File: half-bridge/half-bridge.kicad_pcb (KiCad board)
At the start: 4 copper layers, 59 x 36 mm, 96 parts, among them J1 Conn_01x11_Pin, J2 MountingHole_Pad, J3 Conn_01x11_Pin, J4 Conn_01x11_Pin, J5 Conn_01x11_Pin, J6 Conn_01x11_Pin, J7 MountingHole_Pad, J8 MountingHole_Pad, J9 MountingHole_Pad, Q1 EPC2306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

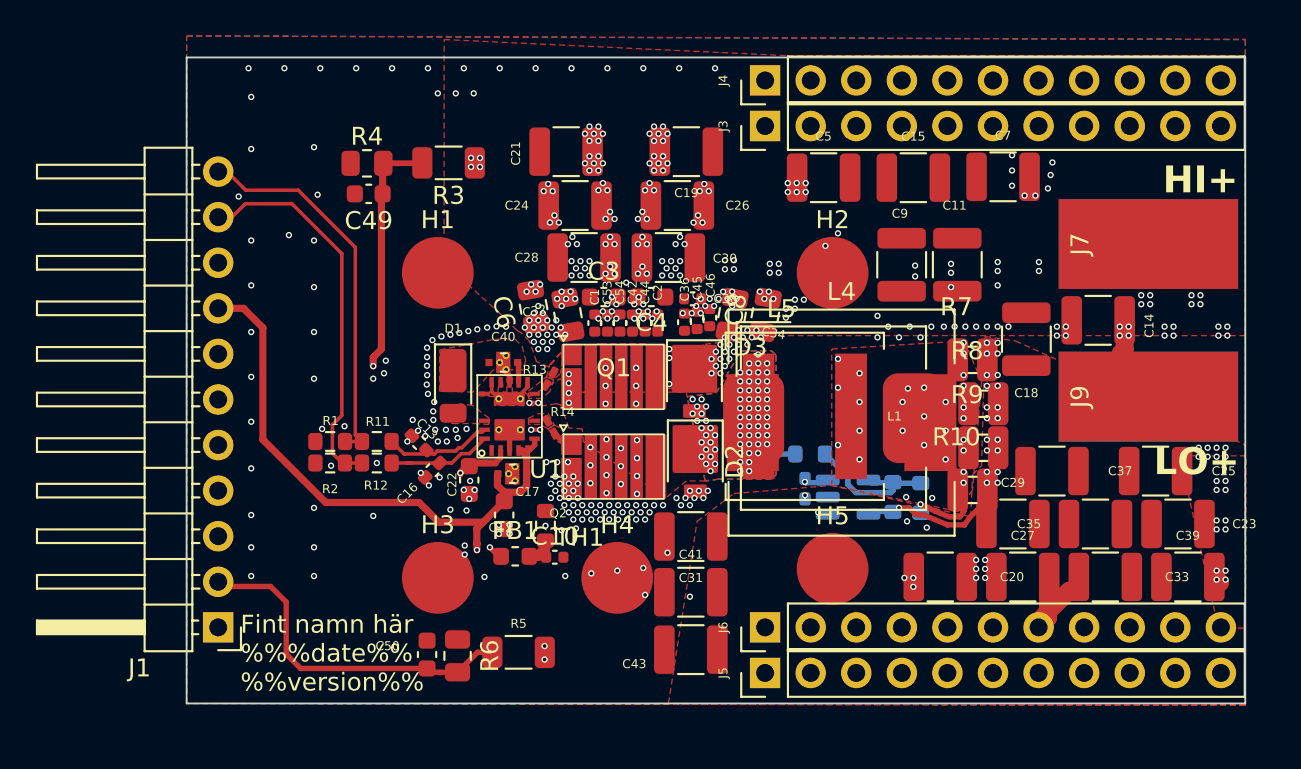
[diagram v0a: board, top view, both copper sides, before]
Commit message: Slightly increase POWER_HIGH area
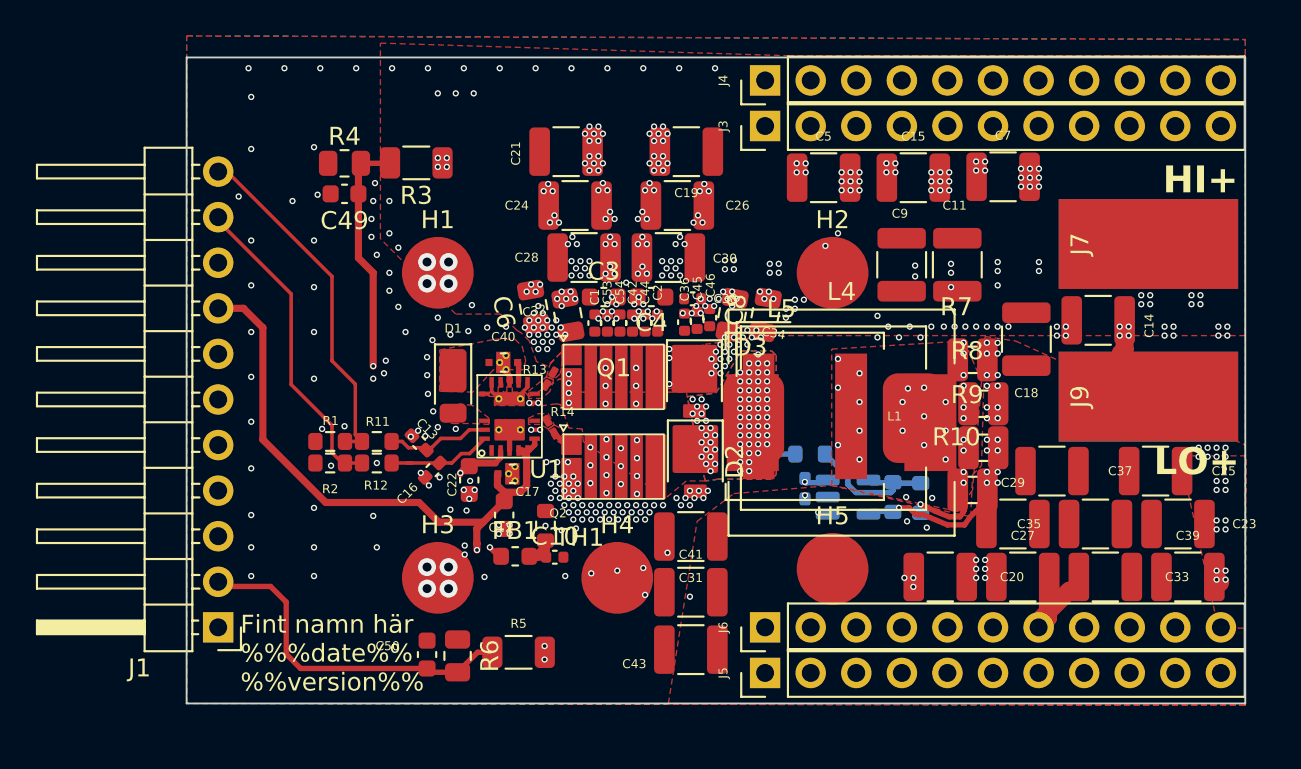
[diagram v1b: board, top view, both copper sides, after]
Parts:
- moved R3 1.80 mm to (122.8, 85.9)
- moved C49 1.35 mm to (118.8, 87.6)
- moved R4 1.25 mm to (118.8, 85.9)
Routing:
- net /LI: track 21.6 -> 17.7 mm
- net FB_HIGH: track 29.6 -> 27.3 mm
- net /HI: track 21.3 -> 19.6 mm
- net 0: track 8.59 -> 8.29 mm, vias 340 -> 369
- net POWER_HIGH: vias 113 -> 117

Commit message: Increase POWER_HIGH area further
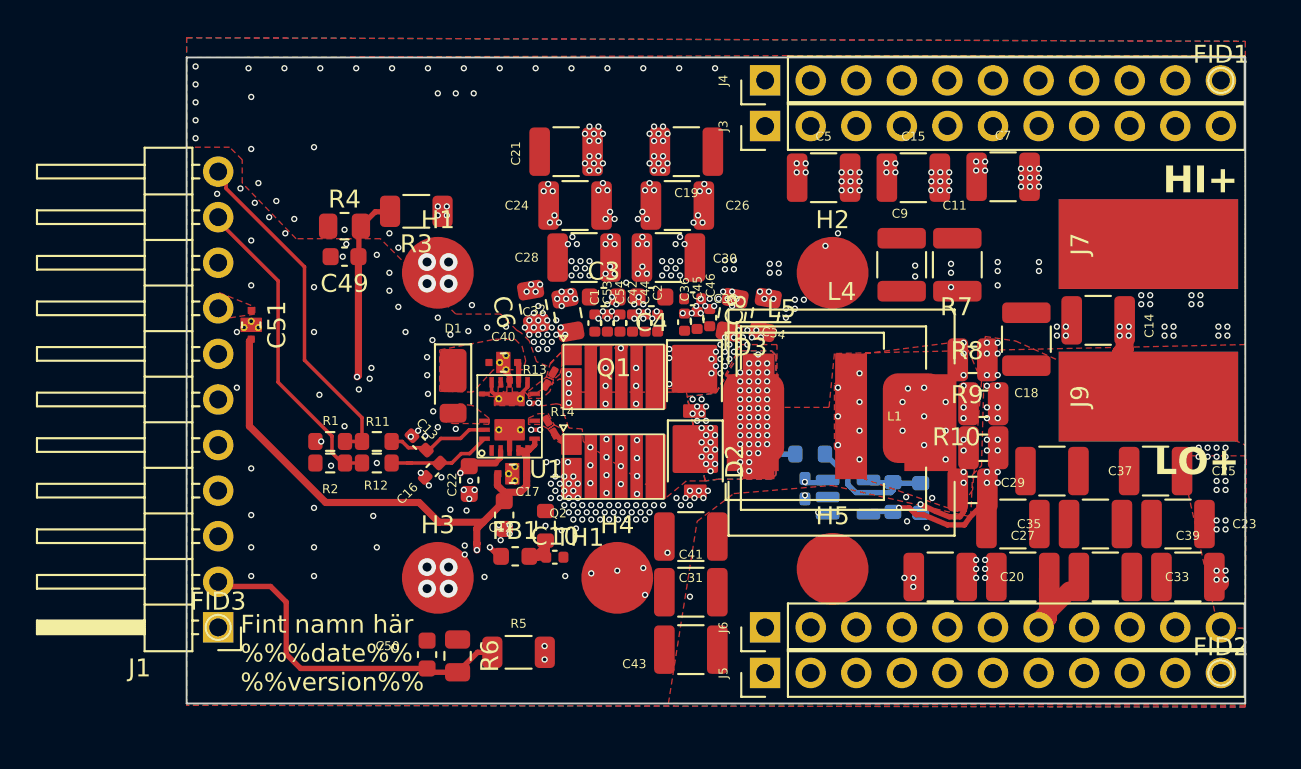
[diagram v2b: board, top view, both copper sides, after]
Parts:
- added C51: YFF18PW0J474M, Library:C_0603_1608Metric_Feedthrough_W_Vias, F.Cu at (113.6, 94.9)
- added FID1: Fiducial, TestPoint:TestPoint_Pad_D1.0mm, F.Cu at (167.6, 81.3)
- added FID2: Fiducial, TestPoint:TestPoint_Pad_D1.0mm, F.Cu at (167.6, 114.3)
- added FID3: Fiducial, TestPoint:TestPoint_Pad_D1.0mm, F.Cu at (111.8, 111.8)
- moved C49 3.50 mm to (118.8, 91.1)
- moved R4 3.50 mm to (118.8, 89.4)
- moved R3 2.70 mm to (122.8, 88.6)
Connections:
- J1 pad 8: +5V -> Net-(J1-Pin_8)
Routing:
- net FB_HIGH: track 27.3 -> 23.2 mm
- net +5V: track 53.8 -> 50.5 mm
- net POWER_HIGH: vias 117 -> 125
- net 0: vias 369 -> 354
- added copper zone on F.Cu, net Net-(J1-Pin_8)

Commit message: Some drc fixes
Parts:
- turned NT1 to 50 degrees
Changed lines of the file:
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@@
 			(at 0 -1.448 0)
 			(layer "F.SilkS")
+			(hide yes)
 			(effects
 				(font
@@
 			)
 		)
-		(pad "1" smd circle
+		(pad "" smd circle
 			(at 0 0)
 			(size 1 1)
-			(layers "F.Cu" "F.Mask")
+			(layers "F.Paste")
 		)
 	)
@@
 		(tags "capacitor")
 		(property "Reference" "C25"
-			(at 3.8 0 0)
+			(at 3.1 0.75 0)
 			(layer "F.SilkS")
 			(effects
@@
 			(at 0 -1.448 0)
 			(layer "F.SilkS")
+			(hide yes)
 			(effects
 				(font
@@
 			)
 		)
-		(pad "1" smd circle
+		(pad "" smd circle
 			(at 0 0)
 			(size 1 1)
-			(layers "F.Cu" "F.Mask")
+			(layers "F.Paste")
 		)
 	)
@@
 		(tags "MesurementPoint Square SMDPad 5mmx10mm ")
 		(property "Reference" "J7"
-			(at 0 -3.81 -90)
+			(at 0 -6.3 0)
 			(layer "F.SilkS")
 			(effects
@@
 			)
 		)
-		(pad "1" smd circle
+		(pad "" smd circle
 			(at 0 0)
 			(size 1 1)
-			(layers "F.Cu" "F.Mask")
+			(layers "F.Paste")
 		)
 	)
@@
 		(tags "MesurementPoint Square SMDPad 5mmx10mm ")
 		(property "Reference" "J9"
-			(at 0 -3.81 -90)
+			(at 3.4 2.5 0)
 			(layer "F.SilkS")
 			(effects
@@
 	(footprint "NetTie:NetTie-2_SMD_Pad0.5mm"
 		(layer "B.Cu")
-		(at 153.845746 105.427927 45)
+		(at 153.845746 105.4 50)
 		(descr "Net tie, 2 pin, 0.5mm square SMD pads")
 		(tags "net tie")
 		(property "Reference" "NT1"
-			(at 0 1.2 45)
+			(at 0 1.2 50)
 			(layer "B.SilkS")
 			(hide yes)
@@
 		)
 		(property "Value" "NetTie_2"
-			(at 0 -1.2 45)
+			(at 0 -1.2 50)
 			(layer "B.Fab")
 			(hide yes)
@@
 		)
 		(property "Footprint" "NetTie:NetTie-2_SMD_Pad0.5mm"
-			(at 0 0 -135)
+			(at 0 0 -130)
 			(unlocked yes)
 			(layer "B.Fab")
@@
 		)
 		(property "Datasheet" ""
-			(at 0 0 -135)
+			(at 0 0 -130)
 			(unlocked yes)
 			(layer "B.Fab")
@@
 		)
 		(property "Description" ""
-			(at 0 0 -135)
+			(at 0 0 -130)
 			(unlocked yes)
 			(layer "B.Fab")
@@
 		)
 		(property "Sim.Device" "R"
-			(at 0 0 -45)
+			(at 0 0 -40)
 			(layer "B.Fab")
 			(hide yes)
@@
 		)
 		(property "Sim.Params" "r=1m"
-			(at 0 0 -45)
+			(at 0 0 -40)
 			(layer "B.Fab")
 			(hide yes)
@@
 		)
 		(property "Sim.Pins" "1=+ 2=-"
-			(at 0 0 -45)
+			(at 0 0 -40)
 			(layer "B.Fab")
 			(hide yes)
@@
 		(fp_poly
 			(pts
-				(xy -0.3 0.15) (xy 0.300001 0.150001) (xy 0.3 -0.15) (xy -0.300001 -0.150001)
+				(xy -0.3 0.149999) (xy 0.300001 0.150001) (xy 0.3 -0.149999) (xy -0.300001 -0.150001)
 			)
 			(stroke
@@
 		)
 		(pad "1" smd circle
-			(at -0.3 0 45)
+			(at -0.3 0 50)
 			(size 0.3 0.3)
 			(layers "F.Cu")
@@
 		)
 		(pad "2" smd circle
-			(at 0.3 0 45)
+			(at 0.3 0 50)
 			(size 0.3 0.3)
 			(layers "F.Cu")
@@
 	)
 	(gr_text "LO+"
-		(at 163.9 103.4 0)
+		(at 164.3 103.4 0)
 		(layer "F.SilkS")
 		(effects
@@
 	)
 	(via
-		(at 110.5 81.5)
+		(at 110.6 81.6)
 		(size 0.35)
 		(drill 0.2)
@@
 	)
 	(via
-		(at 110.5 80.5)
+		(at 110.6 80.6)
 		(size 0.35)
 		(drill 0.2)
@@
 	)
 	(via
-		(at 110.5 83.5)
+		(at 110.6 83.6)
 		(size 0.35)
 		(drill 0.2)
@@
 	)
 	(via
-		(at 110.5 84.5)
+		(at 110.6 84.6)
 		(size 0.35)
 		(drill 0.2)
@@
 	)
 	(via
-		(at 110.5 82.5)
+		(at 110.6 82.6)
 		(size 0.35)
 		(drill 0.2)
@@
 	)
 	(via
-		(at 124.6 109.6)
+		(at 124.6 109.8)
 		(size 1)
 		(drill 0.5)
@@
 	)
 	(via
-		(at 123.4 109.6)
+		(at 123.4 109.8)
 		(size 1)
 		(drill 0.5)
@@
 	)
 	(via
-		(at 124.6 108.4)
+		(at 124.6 108)
 		(size 1)
 		(drill 0.5)
@@
 	)
 	(via
-		(at 123.4 108.4)
+		(at 123.4 108)
 		(size 1)
 		(drill 0.5)
@@
 	)
 	(segment
-		(start 113.38 108.3)
-		(end 111.76 106.68)
+		(start 141.086088 104.5889)
+		(end 143.831156 104.5889)
 		(width 0.3)
 		(layer "In2.Cu")
@@
 	(segment
 		(start 136.480292 106.552)
-		(end 135.1 107.35)
+		(end 139.122988 106.552)
 		(width 0.3)
 		(layer "In2.Cu")
@@
 	)
 	(segment
-		(start 144.83 104.98)
-		(end 144.222256 104.98)
+		(start 127.3389 108.3)
+		(end 127.7 107.9389)
 		(width 0.3)
 		(layer "In2.Cu")
@@
 	)
 	(segment
-		(start 135.1 107.35)
-		(end 130.2 107.95)
+		(start 130.2 107.95)
+		(end 135.1 107.35)
+		(width 0.3)
+		(layer "In2.Cu")
+		(net 24)
+	)
+	(segment
+		(start 126.4 108.3)
+		(end 127.3389 108.3)
 		(width 0.3)
 		(layer "In2.Cu")
@@
 	)
 	(segment
-		(start 141.086088 104.5889)
-		(end 139.122988 106.552)
+		(start 144.222256 104.98)
+		(end 144.83 104.98)
 		(width 0.3)
 		(layer "In2.Cu")
@@
 	)
 	(segment
-		(start 144.222256 104.98)
-		(end 143.831156 104.5889)
+		(start 127.7 107.9389)
+		(end 130.1889 107.9389)
 		(width 0.3)
 		(layer "In2.Cu")
@@
 	)
 	(segment
-		(start 143.831156 104.5889)
-		(end 141.086088 104.5889)
+		(start 135.1 107.35)
+		(end 136.480292 106.552)
 		(width 0.3)
 		(layer "In2.Cu")
@@
 	)
 	(segment
-		(start 130.2 107.95)
-		(end 130.1889 107.9389)
+		(start 113.38 108.3)
+		(end 121.5 108.3)
 		(width 0.3)
 		(layer "In2.Cu")
@@
 	)
 	(segment
-		(start 130.1889 107.9389)
-		(end 127.7 107.9389)
+		(start 111.76 106.68)
+		(end 113.38 108.3)
 		(width 0.3)
 		(layer "In2.Cu")
@@
 	)
 	(segment
-		(start 139.122988 106.552)
-		(end 136.480292 106.552)
+		(start 125.8 108.9)
+		(end 126.4 108.3)
 		(width 0.3)
 		(layer "In2.Cu")
@@
 	)
 	(segment
-		(start 127.7 107.9389)
-		(end 127.3389 108.3)
+		(start 143.831156 104.5889)
+		(end 144.222256 104.98)
 		(width 0.3)
 		(layer "In2.Cu")
@@
 	)
 	(segment
-		(start 127.3389 108.3)
-		(end 113.38 108.3)
+		(start 122.1 108.9)
+		(end 125.8 108.9)
 		(width 0.3)
 		(layer "In2.Cu")
@@
 	)
 	(segment
-		(start 145.2 105.35)
-		(end 144.83 104.98)
+		(start 144.83 104.98)
+		(end 145.2 105.35)
+		(width 0.3)
+		(layer "In2.Cu")
+		(net 24)
+	)
+	(segment
+		(start 139.122988 106.552)
+		(end 141.086088 104.5889)
+		(width 0.3)
+		(layer "In2.Cu")
+		(net 24)
+	)
+	(segment
+		(start 130.1889 107.9389)
+		(end 130.2 107.95)
+		(width 0.3)
+		(layer "In2.Cu")
+		(net 24)
+	)
+	(segment
+		(start 121.5 108.3)
+		(end 122.1 108.9)
 		(width 0.3)
 		(layer "In2.Cu")

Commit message: Change pinout and add voltage regulators to controller
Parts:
- moved C51 2.60 mm to (113.6, 97.5)
- moved C49 1.30 mm to (119.3, 89.9), turned to -90 degrees
- moved R4 1.26 mm to (117.6, 89.8), turned to -90 degrees
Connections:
- C51 pad 1: Net-(J1-Pin_8) -> Net-(J1-Pin_7)
- J1 pad 1: 0 -> FB_LOW
- J1 pad 10: /LI -> /HI
- J1 pad 11: /HI -> FB_HIGH
- J1 pad 2: FB_LOW -> 0
- J1 pad 5: FB_HIGH -> 6-18V
- J1 pad 6: 6-18V -> NTC
- J1 pad 7: NTC -> Net-(J1-Pin_7)
- J1 pad 8: Net-(J1-Pin_8) -> 0
- J1 pad 9: 0 -> /LI
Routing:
- net FB_HIGH: track 23.2 -> 11.6 mm, vias 1 -> 0
- net NTC: track 25.6 -> 22.2 mm
- net FB_LOW: track 19.5 -> 16.8 mm
- net +5V: track 50.5 -> 47.9 mm
- net /LI: track 17.7 -> 16.5 mm
- net /HI: track 19.3 -> 18.2 mm
- net 6-18V: track 19.9 -> 18.8 mm
- net POWER_LOW: vias 32 -> 50
- net POWER_HIGH: vias 125 -> 139
- net 0: vias 354 -> 383
- added copper zone on F.Cu, net Net-(J1-Pin_7)
- removed copper zone on F.Cu, net Net-(J1-Pin_8)

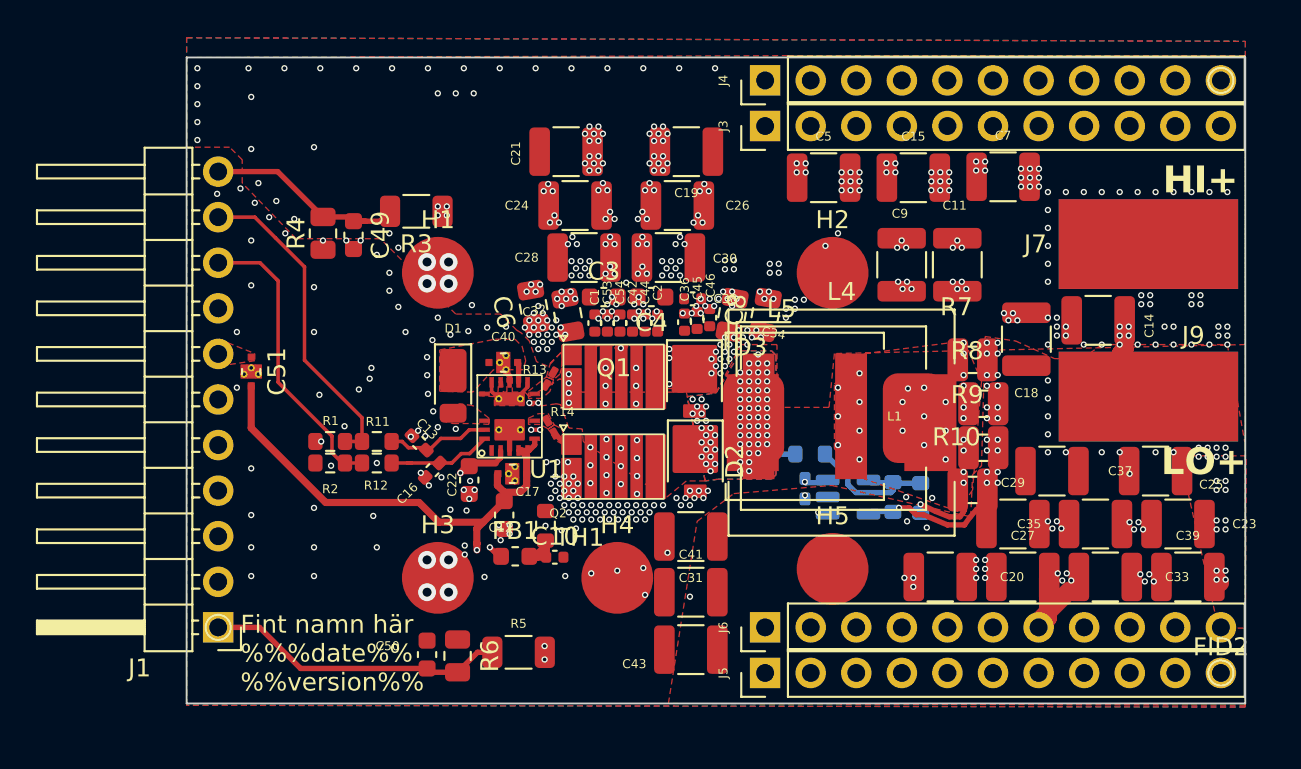
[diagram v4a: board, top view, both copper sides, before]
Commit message: Fixup reference designators, more work on controller etc
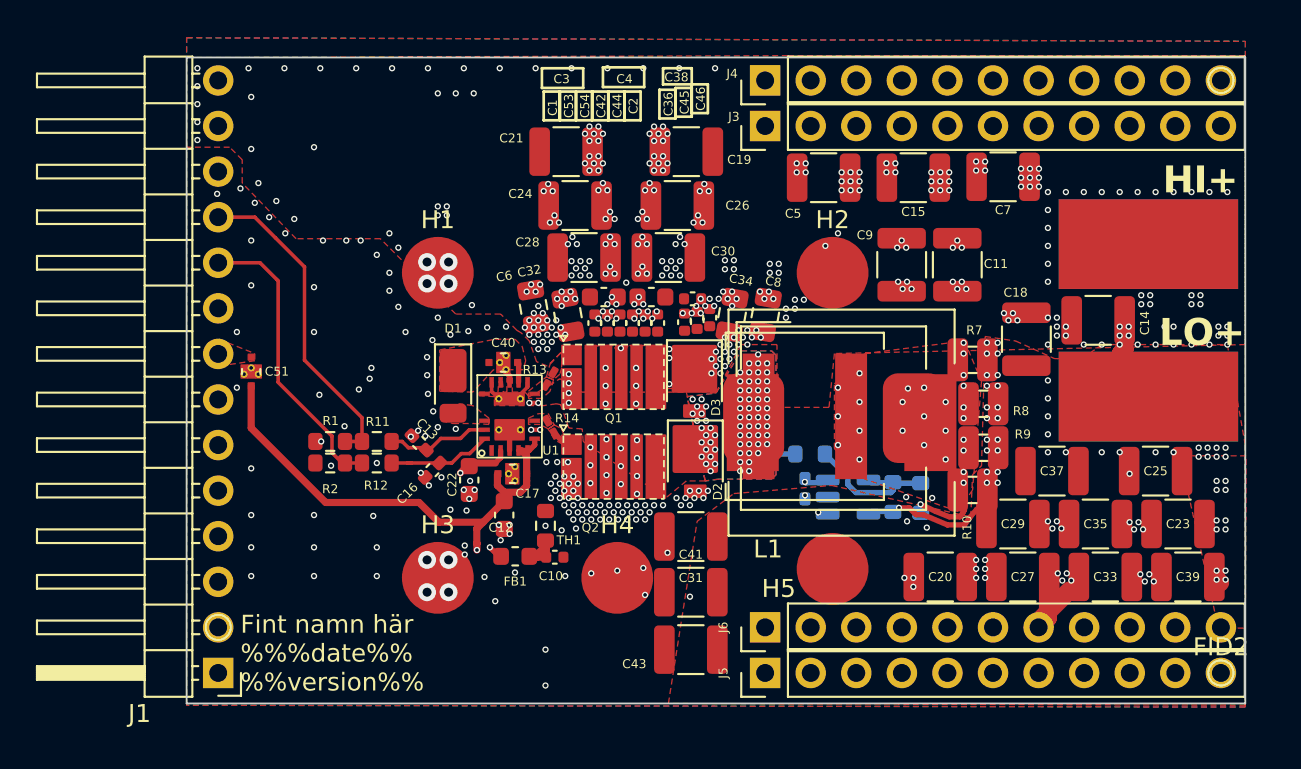
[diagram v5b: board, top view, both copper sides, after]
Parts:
- removed C49, C50: 1nF, Capacitor_SMD:C_0603_1608Metric
- removed R3, R5: 100k, Resistor_SMD:R_1206_3216Metric
- removed R4, R6: 10k, Resistor_SMD:R_0805_2012Metric
- J1: value Conn_01x11_Pin -> Conn_01x14; footprint Connector_PinHeader_2.54mm:PinHeader_1x11_P2.54mm_Horizontal -> Connector_PinHeader_2.54mm:PinHeader_1x14_P2.54mm_Horizontal
- moved J1 2.54 mm to (111.8, 114.3)
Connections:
- C51 pad 1: Net-(J1-Pin_7) -> Net-(J1-Pin_8)
- J1 pad 1: FB_LOW -> 0
- J1 pad 10: /HI -> /LI
- J1 pad 11: FB_HIGH -> /HI
- J1 pad 2: 0 -> POWER_LOW
- J1 pad 3: Current_sense -> 0
- J1 pad 4: 0 -> Current_sense
- J1 pad 5: 6-18V -> 0
- J1 pad 6: NTC -> 6-18V
- J1 pad 7: Net-(J1-Pin_7) -> NTC
- J1 pad 8: 0 -> Net-(J1-Pin_8)
- J1 pad 9: /LI -> 0
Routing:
- net FB_LOW: track 16.8 -> 0.00 mm
- net FB_HIGH: track 11.6 -> 0.00 mm
- net 0: vias 383 -> 386
- added copper zone on F.Cu, net Net-(J1-Pin_8)
- removed copper zone on F.Cu, net Net-(J1-Pin_7)

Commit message: WIP - Reduce size and bump to 6 layers
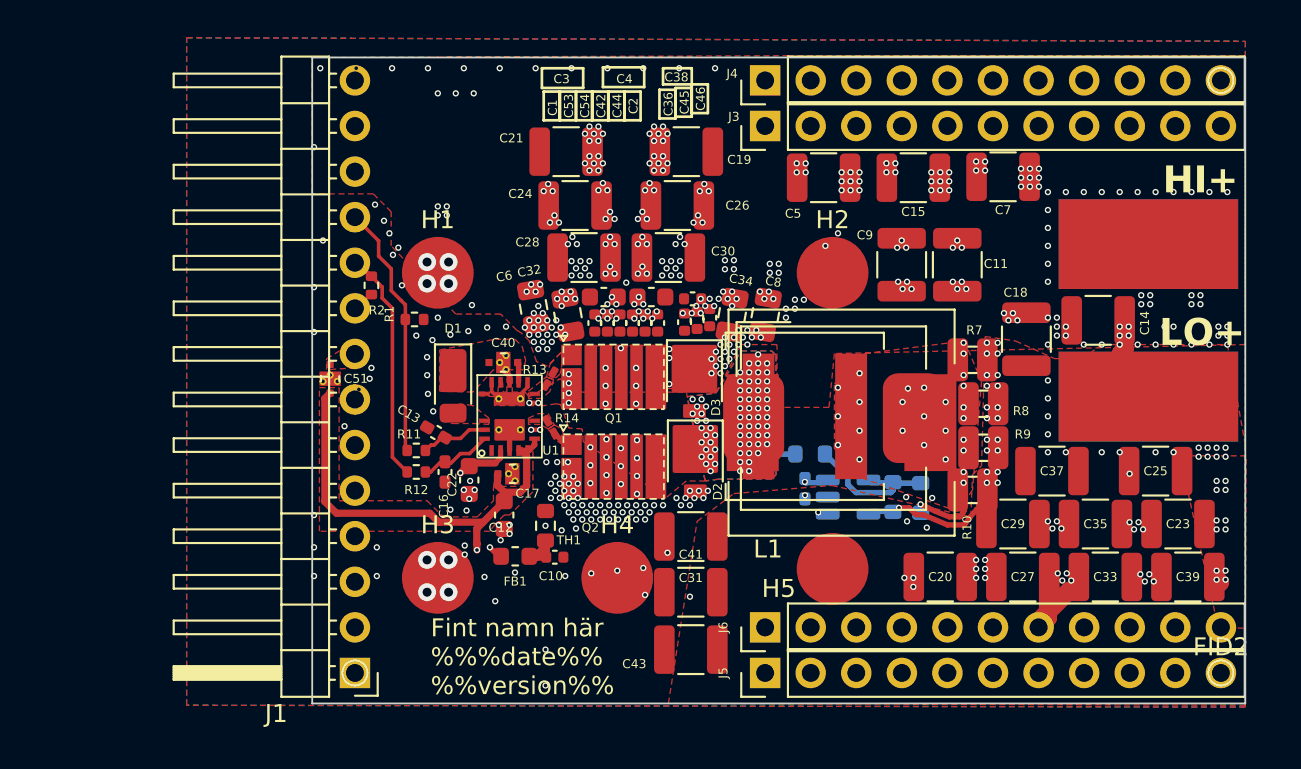
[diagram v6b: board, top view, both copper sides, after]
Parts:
- R1, R11, R12, R2: footprint Resistor_SMD:R_0603_1608Metric -> Resistor_SMD:R_0402_1005Metric
- moved R2 10.2 mm to (120.3, 92.7), turned to 90 degrees
- moved R1 8.27 mm to (122.7, 94.6), turned to 180 degrees
- moved FID3 8.03 mm to (119.4, 114.3)
- moved J1 7.62 mm to (119.4, 114.3)
- moved C51 4.42 mm to (118.0, 97.9)
- moved R11 2.26 mm to (122.8, 101.9)
- moved R12 2.26 mm to (122.8, 103.1)
- moved C13 1.10 mm to (123.9, 100.9), turned to 150 degrees
- moved C16 0.71 mm to (124.4, 103.1), turned to -90 degrees
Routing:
- net 6-18V: track 18.8 -> 9.53 mm
- net Current_sense: track 36.4 -> 28.7 mm
- net NTC: track 22.2 -> 14.6 mm
- net /HI: track 18.2 -> 14.2 mm
- net /LI: track 16.5 -> 13.0 mm
- net Net-(U1-EN/HI): track 5.73 -> 3.61 mm
- net +5V: track 47.9 -> 45.9 mm
- net Net-(U1-PWM/LO): track 6.01 -> 4.06 mm
- net 0: track 8.29 -> 7.39 mm, vias 386 -> 354
- net POWER_HIGH: vias 139 -> 131
- added copper zone on F.Cu, net +5V
- added copper zone on In3.Cu, net 0
- added copper zone on In4.Cu, net 0
- added copper zone on In4.Cu, net POWER_LOW
- added copper zone on In3.Cu, net Switch_node
- added copper zone on In4.Cu, net Switch_node
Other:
- board size 59 x 36 mm -> 52 x 36 mm
- copper layers 4 -> 6
